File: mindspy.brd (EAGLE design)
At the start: 45.7 x 50.8 mm, 39 parts, among them IC1 ADS1298, IC2 TPS7A4901, X1 DF9-31S, X2 STELLARIS-LAUNCHPAD-HALF

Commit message: change packag for ADS1298 (HTQFP-64-PAP -> LQFP64)
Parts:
- IC1: value ADS1298 -> ADS1298IPAG; device fabhack:HTQFP-64-PAP -> ti:LQFP64
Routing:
- net DGND: track 13.2 -> 7.99 mm
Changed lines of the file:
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@@
 </autorouter>
 <elements>
-<element name="IC1" library="fabhack" package="HTQFP-64-PAP" value="ADS1298" x="19.05" y="30.48">
-<attribute name="OC_NEWARK" value="" x="38.1" y="-30.48" size="1.778" layer="27" display="off"/>
-<attribute name="MPN" value="ADS1294IPAG" x="38.1" y="-30.48" size="1.778" layer="27" display="off"/>
-<attribute name="MF" value="" x="38.1" y="-30.48" size="1.778" layer="27" display="off"/>
-<attribute name="OC_FARNELL" value="" x="38.1" y="-30.48" size="1.778" layer="27" display="off"/>
-</element>
+<element name="IC1" library="ti" package="LQFP64" value="ADS1298IPAG" x="19.05" y="30.48"/>
 <element name="X2" library="ti" package="LAUNCHPAD-L" value="STELLARIS-LAUNCHPAD-HALF" x="0" y="0"/>
 <element name="C1" library="rcl" package="SMC_A" value="10u" x="8.89" y="7.62"/>
@@
 <contactref element="IC1" pad="41"/>
 <contactref element="X4" pad="5"/>
-<wire x1="24.75" y1="30.73" x2="27.2375" y2="30.73" width="0.15" layer="1"/>
-<wire x1="27.2375" y1="30.73" x2="27.305" y2="30.7975" width="0.15" layer="1"/>
-<wire x1="24.75" y1="26.73" x2="27.245" y2="26.73" width="0.15" layer="1"/>
-<wire x1="27.245" y1="26.73" x2="27.305" y2="26.67" width="0.15" layer="1"/>
 <wire x1="21.8" y1="36.18" x2="21.8" y2="37.055" width="0.254" layer="1"/>
 <wire x1="21.8" y1="37.055" x2="22.21" y2="37.465" width="0.254" layer="1" curve="-90"/>

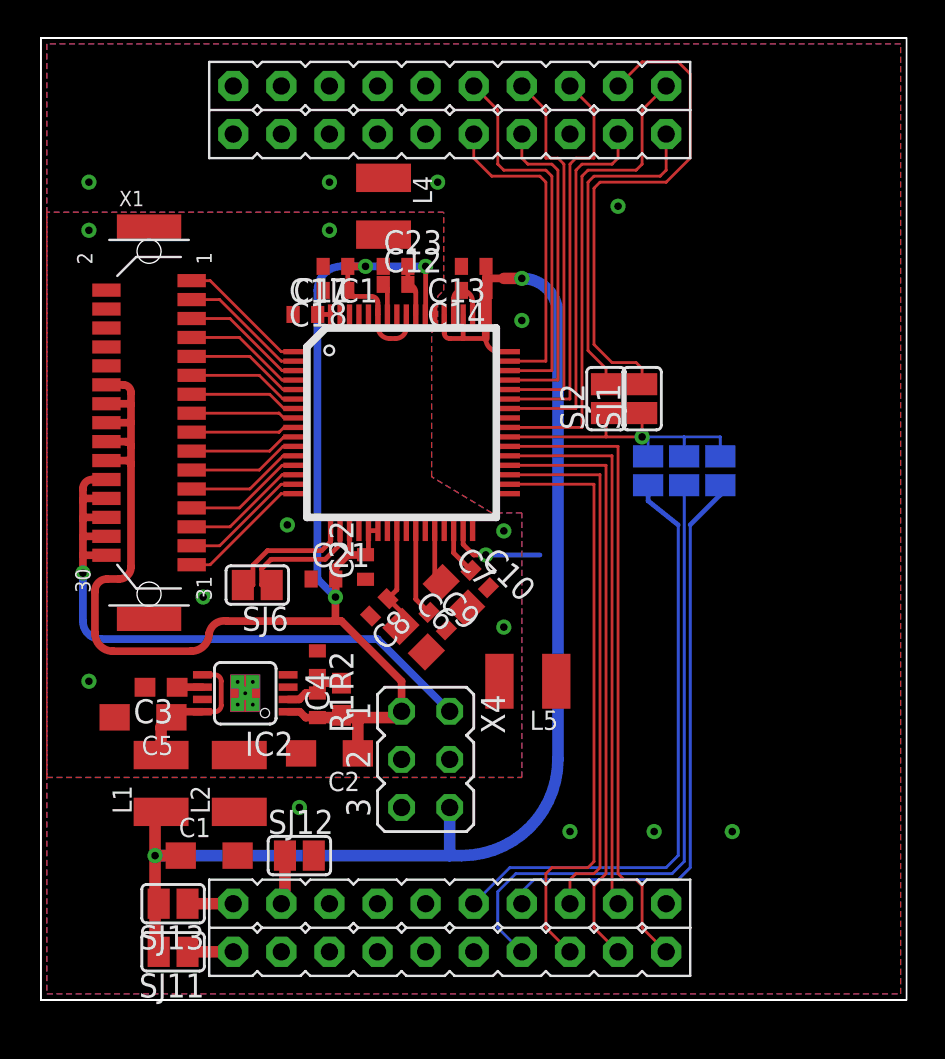
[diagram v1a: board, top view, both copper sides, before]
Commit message: add pads for RLD auxiliary input and rearrange wires
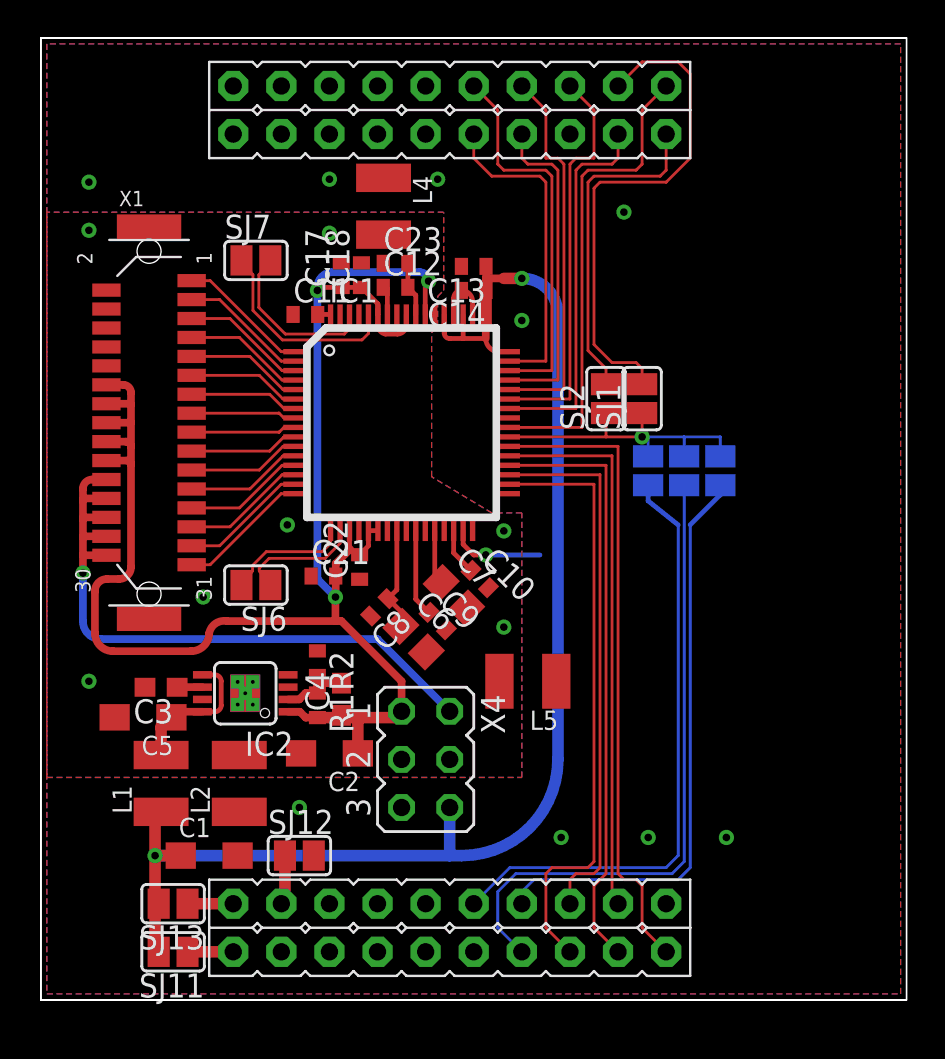
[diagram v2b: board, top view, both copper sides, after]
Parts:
- added SJ7: (no value), jumper:SJ
- moved C18 1.59 mm to (16.9, 38.3), turned to 90 degrees
- moved C17 0.56 mm to (15.9, 38.3), turned to 90 degrees
- moved C22 0.31 mm to (16.8, 22.9)
- moved C23 0.16 mm to (18.7, 38.9)
- moved C12 0.16 mm to (18.7, 37.6)
- moved C21 0.16 mm to (14.9, 22.4)
- moved SJ6 0.07 mm to (11.4, 21.9)
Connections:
- net RLDIN: now also SJ7.2
- net RLDREF: now also SJ7.1
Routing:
- net RLDREF: track 0.00 -> 10.7 mm
- net RLDIN: track 0.00 -> 8.93 mm
- net AVDD: track 90.8 -> 89.4 mm
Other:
- board text added: "AIN1"
- board text added: "AIN8"
- board text added: "RLDIN"
- board text added: "RLDREF"
- board text added: "TESTN"
- board text added: "TESTP"

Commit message: finalization, fixes in layers
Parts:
- IC2: device fabhack:MSOP08 -> ti:MSOP08
- X1: device con-hirose:DF9-31S -> hirose:DF9-31S
- moved SJ4 2.03 mm to (36.0, 27.8)
- moved SJ3 1.87 mm to (34.0, 27.8)
- moved SJ2 0.35 mm to (30.2, 31.6)
- moved SJ1 0.35 mm to (32.1, 31.6)
- moved C11 0.22 mm to (13.8, 36.4)
- moved SJ5 0.16 mm to (32.1, 27.8)
- moved C1 0.16 mm to (9.05, 7.62)
- moved C10 0.16 mm to (23.0, 22.2)
- moved C12 0.16 mm to (18.7, 37.8)
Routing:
- net MOSI: track 31.8 -> 30.9 mm
- net !CS3: track 30.9 -> 30.2 mm
- net !CS4: track 34.1 -> 33.4 mm
- net GPIO4: track 20.3 -> 19.7 mm
- net !PWDN: track 28.6 -> 28.0 mm
- net !DRDY: track 17.0 -> 16.4 mm
- net !CS2: track 17.4 -> 16.8 mm

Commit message: fix part values
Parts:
- C11: value 1n -> 4n7
- C7: value 22u -> 18u
- R1: value (none) -> 24k
- R2: value (none) -> 10k
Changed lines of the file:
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@@
 <grid distance="0.155575" unitdist="mm" unit="mm" style="dots" multiple="1" display="yes" altdistance="0.155575" altunitdist="mm" altunit="mm"/>
 <layers>
-<layer number="1" name="Top" color="4" fill="1" visible="yes" active="yes"/>
-<layer number="16" name="Bottom" color="1" fill="1" visible="yes" active="yes"/>
+<layer number="1" name="Top" color="4" fill="1" visible="no" active="yes"/>
+<layer number="16" name="Bottom" color="1" fill="1" visible="no" active="yes"/>
 <layer number="17" name="Pads" color="2" fill="1" visible="yes" active="yes"/>
 <layer number="18" name="Vias" color="2" fill="1" visible="yes" active="yes"/>
 <layer number="19" name="Unrouted" color="6" fill="1" visible="yes" active="yes"/>
 <layer number="20" name="Dimension" color="15" fill="1" visible="yes" active="yes"/>
-<layer number="21" name="tPlace" color="7" fill="1" visible="no" active="yes"/>
-<layer number="22" name="bPlace" color="7" fill="1" visible="no" active="yes"/>
+<layer number="21" name="tPlace" color="7" fill="1" visible="yes" active="yes"/>
+<layer number="22" name="bPlace" color="7" fill="1" visible="yes" active="yes"/>
 <layer number="23" name="tOrigins" color="15" fill="1" visible="yes" active="yes"/>
 <layer number="24" name="bOrigins" color="15" fill="1" visible="yes" active="yes"/>
@@
 <layer number="27" name="tValues" color="7" fill="1" visible="no" active="yes"/>
 <layer number="28" name="bValues" color="7" fill="1" visible="no" active="yes"/>
-<layer number="29" name="tStop" color="7" fill="3" visible="yes" active="yes"/>
-<layer number="30" name="bStop" color="7" fill="6" visible="yes" active="yes"/>
-<layer number="31" name="tCream" color="7" fill="4" visible="yes" active="yes"/>
-<layer number="32" name="bCream" color="7" fill="5" visible="yes" active="yes"/>
-<layer number="33" name="tFinish" color="6" fill="3" visible="yes" active="yes"/>
-<layer number="34" name="bFinish" color="6" fill="6" visible="yes" active="yes"/>
-<layer number="35" name="tGlue" color="7" fill="4" visible="yes" active="yes"/>
-<layer number="36" name="bGlue" color="7" fill="5" visible="yes" active="yes"/>
-<layer number="37" name="tTest" color="7" fill="1" visible="yes" active="yes"/>
-<layer number="38" name="bTest" color="7" fill="1" visible="yes" active="yes"/>
-<layer number="39" name="tKeepout" color="4" fill="11" visible="yes" active="yes"/>
-<layer number="40" name="bKeepout" color="1" fill="11" visible="yes" active="yes"/>
-<layer number="41" name="tRestrict" color="4" fill="10" visible="yes" active="yes"/>
-<layer number="42" name="bRestrict" color="1" fill="10" visible="yes" active="yes"/>
-<layer number="43" name="vRestrict" color="2" fill="10" visible="yes" active="yes"/>
-<layer number="44" name="Drills" color="7" fill="1" visible="yes" active="yes"/>
-<layer number="45" name="Holes" color="7" fill="1" visible="yes" active="yes"/>
+<layer number="29" name="tStop" color="7" fill="3" visible="no" active="yes"/>
+<layer number="30" name="bStop" color="7" fill="6" visible="no" active="yes"/>
+<layer number="31" name="tCream" color="7" fill="4" visible="no" active="yes"/>
+<layer number="32" name="bCream" color="7" fill="5" visible="no" active="yes"/>
+<layer number="33" name="tFinish" color="6" fill="3" visible="no" active="yes"/>
+<layer number="34" name="bFinish" color="6" fill="6" visible="no" active="yes"/>
+<layer number="35" name="tGlue" color="7" fill="4" visible="no" active="yes"/>
+<layer number="36" name="bGlue" color="7" fill="5" visible="no" active="yes"/>
+<layer number="37" name="tTest" color="7" fill="1" visible="no" active="yes"/>
+<layer number="38" name="bTest" color="7" fill="1" visible="no" active="yes"/>
+<layer number="39" name="tKeepout" color="4" fill="11" visible="no" active="yes"/>
+<layer number="40" name="bKeepout" color="1" fill="11" visible="no" active="yes"/>
+<layer number="41" name="tRestrict" color="4" fill="10" visible="no" active="yes"/>
+<layer number="42" name="bRestrict" color="1" fill="10" visible="no" active="yes"/>
+<layer number="43" name="vRestrict" color="2" fill="10" visible="no" active="yes"/>
+<layer number="44" name="Drills" color="7" fill="1" visible="no" active="yes"/>
+<layer number="45" name="Holes" color="7" fill="1" visible="no" active="yes"/>
 <layer number="46" name="Milling" color="3" fill="1" visible="yes" active="yes"/>
 <layer number="47" name="Measures" color="7" fill="1" visible="yes" active="yes"/>
-<layer number="48" name="Document" color="7" fill="1" visible="yes" active="yes"/>
+<layer number="48" name="Document" color="7" fill="1" visible="no" active="yes"/>
 <layer number="49" name="Reference" color="7" fill="1" visible="yes" active="yes"/>
 <layer number="50" name="dxf" color="7" fill="1" visible="no" active="no"/>
-<layer number="51" name="tDocu" color="7" fill="1" visible="no" active="yes"/>
+<layer number="51" name="tDocu" color="7" fill="1" visible="yes" active="yes"/>
 <layer number="52" name="bDocu" color="7" fill="1" visible="no" active="yes"/>
 <layer number="53" name="tGND_GNDA" color="7" fill="9" visible="no" active="no"/>
@@
 <element name="C5" library="rcl" package="SMC_A" value="10u" x="5.3975" y="14.9225" rot="R180"/>
 <element name="C6" library="rcl" package="C0805" value="10u" x="19.685" y="19.05" rot="R315"/>
-<element name="C7" library="rcl" package="C0805" value="22u" x="21.81450625" y="21.365490625" rot="R315"/>
+<element name="C7" library="rcl" package="C0805" value="18u" x="21.81450625" y="21.365490625" rot="R315"/>
 <element name="C8" library="rcl" package="C0402" value="0.1u" x="17.872990625" y="20.730490625" rot="R225"/>
 <element name="C9" library="rcl" package="C0402" value="1u" x="20.955" y="20.0025" rot="R315"/>
-<element name="C11" library="rcl" package="C0402" value="1n" x="13.814425" y="36.350575"/>
+<element name="C11" library="rcl" package="C0402" value="4n7" x="13.814425" y="36.350575"/>
 <element name="C12" library="rcl" package="C0402" value="0.1u" x="18.7325" y="37.7825"/>
 <element name="C13" library="rcl" package="C0402" value="1u" x="22.86" y="38.735" rot="R180"/>
@@
 <element name="SJ13" library="jumper" package="SJ" value="" x="6.985" y="5.08" rot="R180"/>
 <element name="IC2" library="ti" package="MSOP08" value="TPS7A4901" x="10.795" y="16.1925" rot="R90"/>
-<element name="R1" library="rcl" package="R0402" value="" x="14.605" y="15.5575" rot="R270"/>
-<element name="R2" library="rcl" package="R0402" value="" x="14.605" y="17.78" rot="R270"/>
+<element name="R1" library="rcl" package="R0402" value="24k" x="14.605" y="15.5575" rot="R270"/>
+<element name="R2" library="rcl" package="R0402" value="10k" x="14.605" y="17.78" rot="R270"/>
 <element name="C2" library="rcl" package="SMC_A" value="10u" x="15.24" y="13.0175" rot="R180"/>
 <element name="X4" library="jumper" package="JP3Q" value="" x="20.32" y="12.7" rot="R270"/>
@@
 </signal>
 </signals>
-<errors>
-</errors>
 </board>
 </drawing>

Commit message: Major changes
* placing improvements
 * labels on board
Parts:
- removed L4, L5: 10u, fabhack:L1210K
- moved C21 0.64 mm to (14.8, 21.8)
- moved C23 0.49 mm to (18.6, 38.4)
- moved C17 0.49 mm to (15.7, 37.8)
- moved SJ7 0.49 mm to (11.2, 38.6)
- moved C14 0.49 mm to (22.7, 37.0)
- moved C18 0.49 mm to (16.8, 37.8)
- moved C22 0.49 mm to (16.7, 22.4)
- moved C7 0.49 mm to (21.7, 20.9)
- moved IC1 0.49 mm to (18.9, 30.0)
- moved C2 0.49 mm to (15.1, 12.6)
- moved SJ12 0.49 mm to (13.5, 7.15)
- moved SJ13 0.49 mm to (6.83, 4.61)
- moved SJ6 0.49 mm to (11.2, 21.4)
- moved C3 0.49 mm to (6.19, 16.0)
- moved C5 0.49 mm to (5.24, 14.5)
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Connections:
- net AVCM: now also X1.12, X1.18, X1.6; no longer X1.22, X1.26, X1.28
- net AVDD: now also X1.10, X1.22, X1.28, X1.4; no longer X1.12, X1.14, X1.18, X1.20
- net AVSS: now also X1.14, X1.20, X1.26; no longer L4.2, L5.2, X1.10, X1.4, X1.6
- net DGND: no longer L4.1, L5.1
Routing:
- net AVDD: track 89.4 -> 30.6 mm, vias 3 -> 8
- net DVDD: track 73.2 -> 20.2 mm
- net AVCM: track 34.8 -> 42.7 mm
- net DGND: track 7.99 -> 7.12 mm, vias 10 -> 0
- net AVSS: vias 7 -> 0
- added copper zone on layer 16, net AVDD
- added copper zone on layer 16, net DVDD
- removed copper zone on layer 16, net DGND
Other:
- board text added: "+"
- board text added: "-"
- board text added: "0V"
- board text added: "100uH"
- board text added: "10k"
- board text added: "10n"
- board text added: "10u"
- board text added: "18u"
- board text added: "1u"
- board text added: "24k"
- board text added: "3V3"
- board text added: "4n7"
- board text added: "5V"
- board text added: "RLDREF/IN"
- board text added: "TESTP/N"
- board text added: "u1"
- board text added: "ver. 0.2"
- board text removed: "RLDIN"
- board text removed: "RLDREF"
- board text removed: "TESTN"
- board text removed: "TESTP"
- board text removed: "ver. 0.1"
